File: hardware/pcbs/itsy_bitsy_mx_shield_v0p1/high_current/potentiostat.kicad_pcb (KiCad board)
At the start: 2 copper layers, 144.8 x 88.9 mm, 139 parts, among them K1 Conn_01x03, P1 Conn_01x02, P10 Conn_01x02, P11 Conn_01x02, P12 Conn_01x02, P13 Conn_02x05_Odd_Even, P14 Conn_02x05_Odd_Even, P15 Conn_02x02_Odd_Even, P16 Conn_02x02_Odd_Even, P17 Conn_01x02, P18 Conn_01x02, P19 Conn_01x02, P2 Conn_01x02, P20 Conn_01x02, P21 Conn_01x02, P22 Conn_01x02, P3 Conn_01x02, P4 Conn_01x02, P5 Conn_01x02, P6 Conn_01x02, P7 Conn_01x02, P8 Conn_01x02, P9 Conn_01x02, U1 74HC138, U11 OP07, U12 OP07, U13 OP07, U14 OP07, U15 OP07, U16 OP07, U17 OP07, U18 OP07, U19 74HC138, U2 ITSY_BITSY_M4, U20 OP07, U21 74HC138, U3 DG411xY, U4 DG411xY, U5 DG411xY, U6 MEA1D05XXSC, U7 DG411xY, U8 DG411xY, U9 TL072

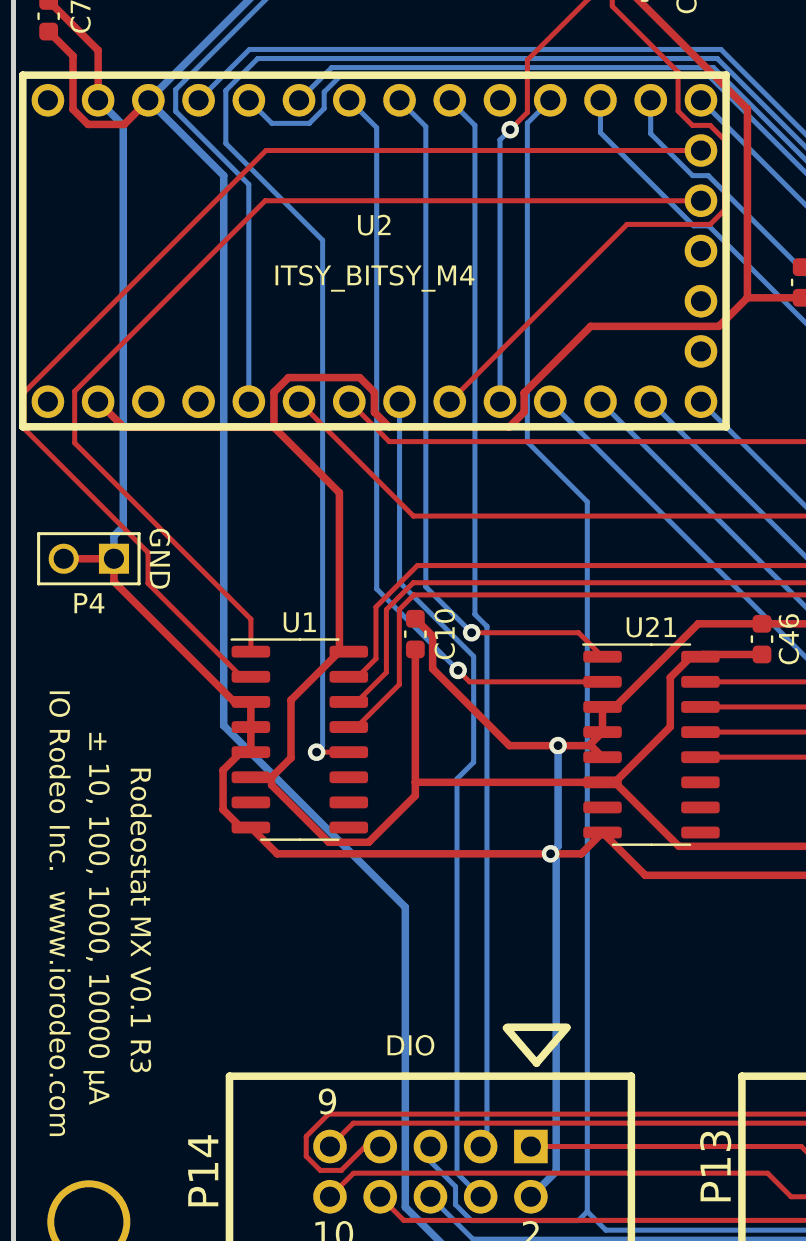
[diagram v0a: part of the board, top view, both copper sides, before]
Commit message: Added fab files to include through hole assembly.
Increased revision number V0.1 R4.  Remade gerbers to include addtional
elements on silkscreen.
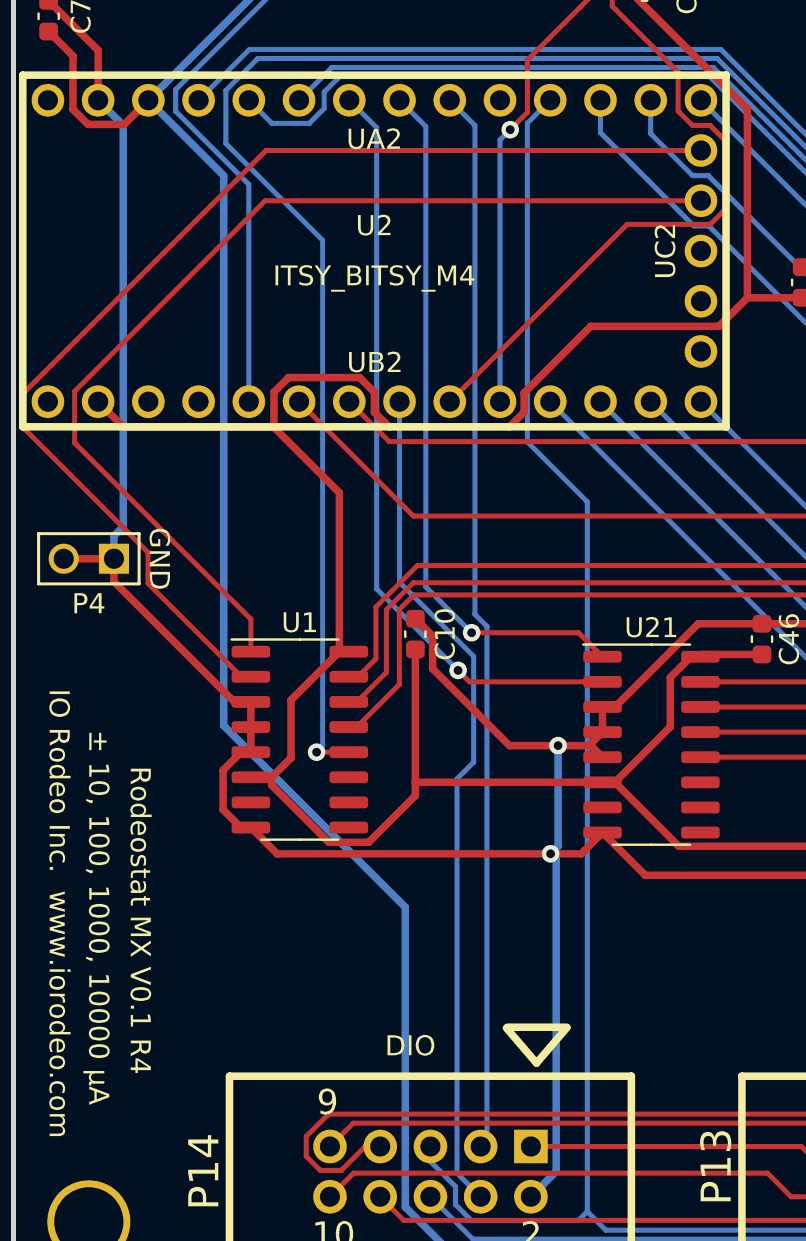
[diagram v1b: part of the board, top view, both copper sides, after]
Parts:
- added UA2: header_14_pos, dummy:header_14_pos, F.Cu at (69.0, 79.2)
- added UB2: header_14_pos, dummy:header_14_pos, F.Cu at (69.0, 94.4)
- added UC2: header_5_pos, dummy:header_5_pos, F.Cu at (85.6, 86.8)
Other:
- board text added: "Rodeostat MX V0.1 R4"
- board text removed: "Rodeostat MX V0.1 R3"
